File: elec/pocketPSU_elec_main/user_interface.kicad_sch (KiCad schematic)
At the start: 34 parts, among them J3 Conn_01x12_Pin, SW1 EC11E09244BS, U1 2N7002_C5224215

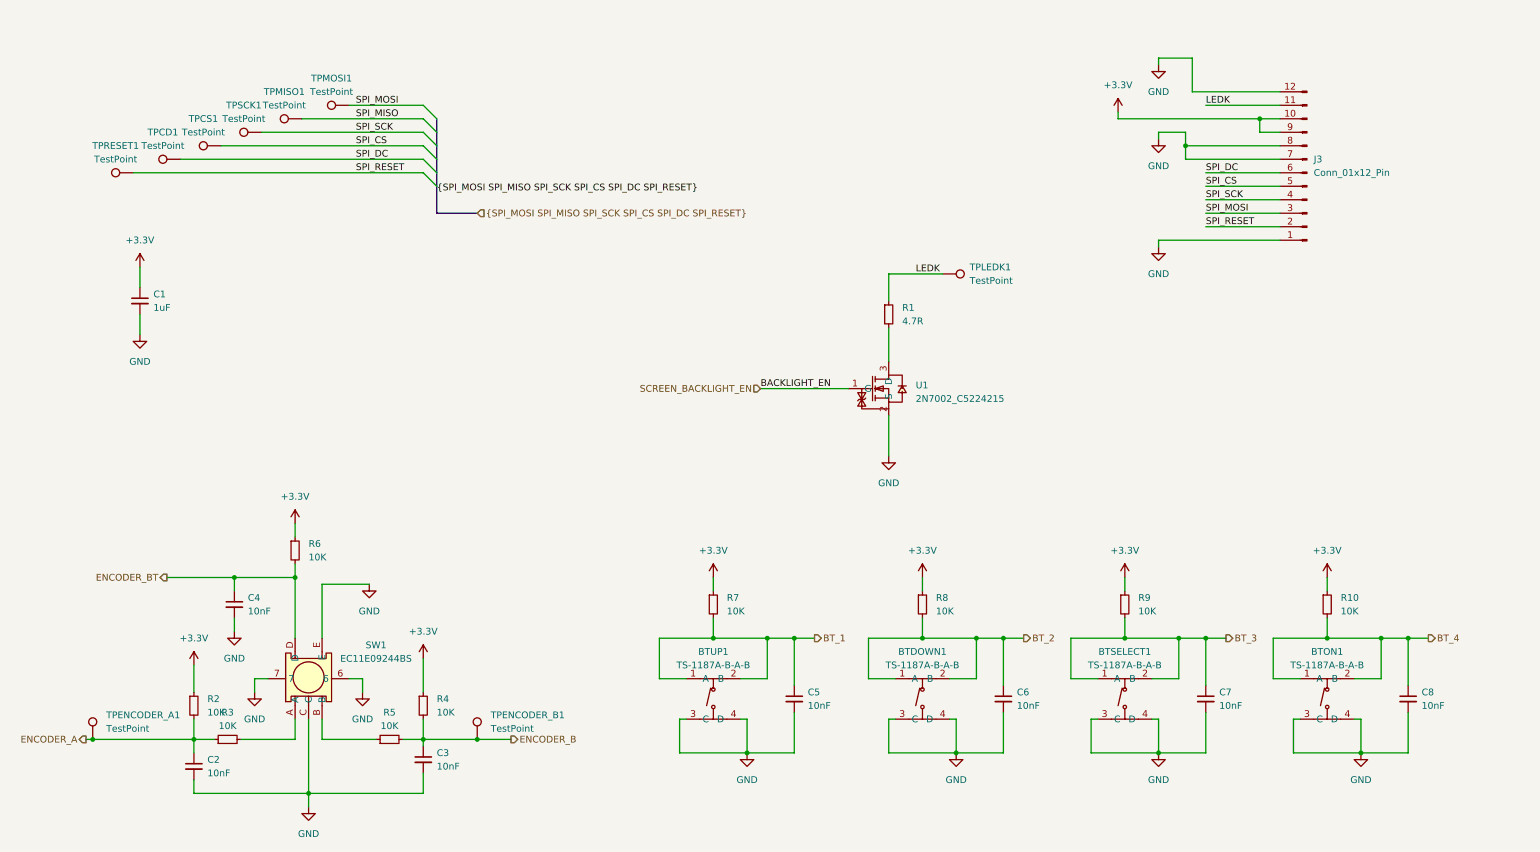
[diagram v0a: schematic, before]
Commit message: add buttons and leds for on/off indication
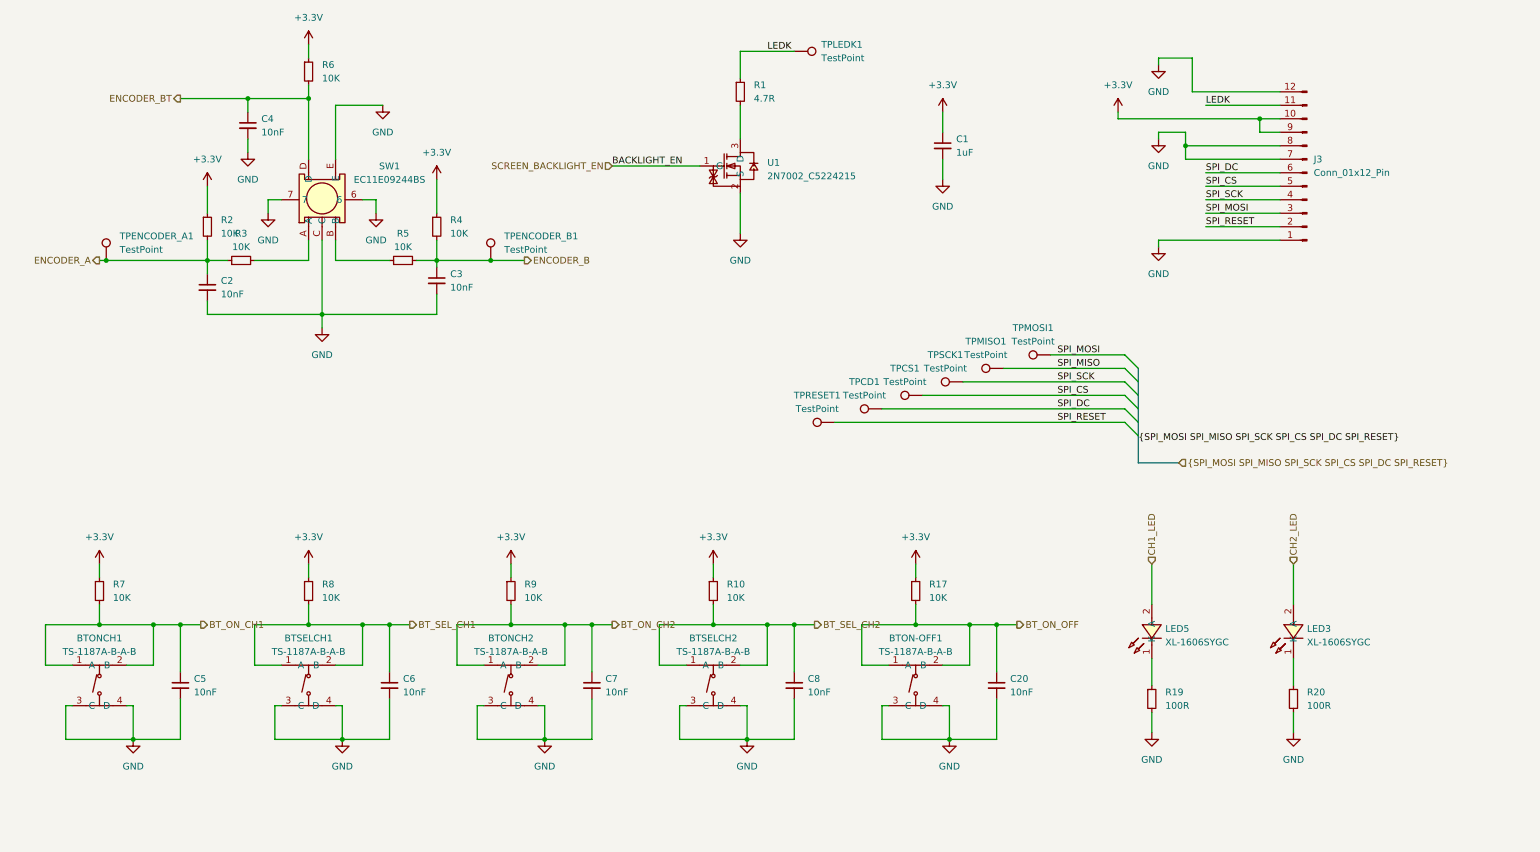
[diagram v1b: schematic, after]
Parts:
- added BTON-OFF1: TS-1187A-B-A-B, footprints:SW-SMD_4P-L5.1-W5.1-P3.70-LS6.5-TL-2, symbol footprints:TS-1187A-B-A-B
- added C20: 10nF, Capacitor_SMD:C_0402_1005Metric, symbol Device:C_Small
- added LED3, LED5: XL-1606SYGC, footprints:LED-SMD_L1.7-W1.1-RD_27-21, symbol footprints:XL-1606SYGC
- added R17: 10K, Resistor_SMD:R_0402_1005Metric, symbol Device:R_Small
- added R19, R20: 100R, Resistor_SMD:R_0402_1005Metric, symbol Device:R_Small
- renumbered BTUP1 to BTONCH1, BTSELECT1 to BTONCH2, BTDOWN1 to BTSELCH1, BTON1 to BTSELCH2
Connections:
- net +3.3V: now also R17.1
- net GND: now also BTON-OFF1.3 (C), BTON-OFF1.4 (D), C20.2, R19.2, R20.2
- net BT_1 renamed BT_ON_CH1
- net BT_2 renamed BT_SEL_CH1
- net BT_3 renamed BT_ON_CH2
- net BT_4 renamed BT_SEL_CH2
- new net: LED3.1 (K), R20.1
- new net: LED5.1 (K), R19.1
- new net BT_ON_OFF: BTON-OFF1.1 (A), BTON-OFF1.2 (B), C20.1, R17.2
- new net CH1_LED: LED5.2 (A)
- new net CH2_LED: LED3.2 (A)
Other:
- moved on the sheet: BTONCH1, BTONCH2, BTSELCH1, BTSELCH2, C1, C2, C3, C4, C5, C6, C7, C8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

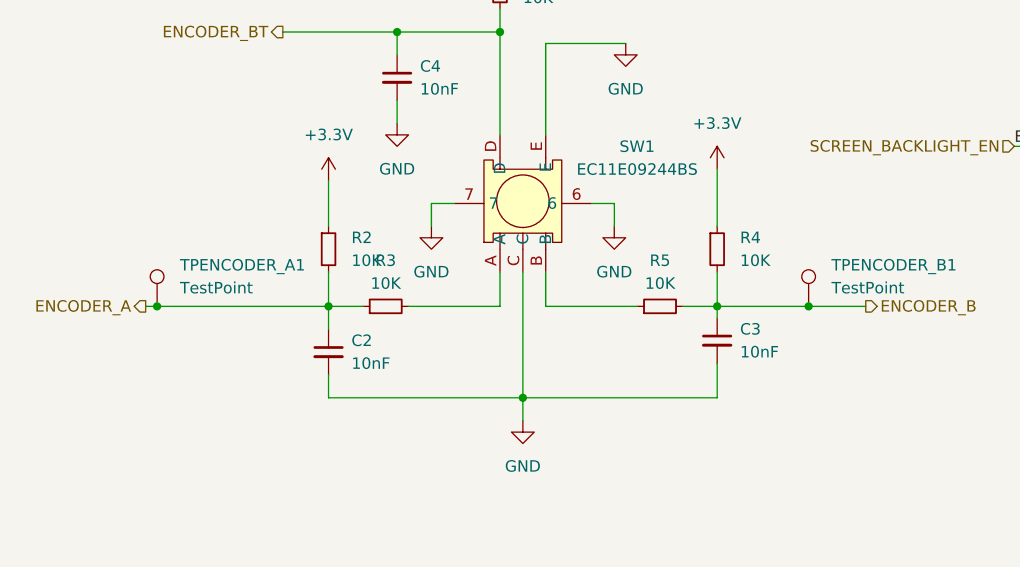
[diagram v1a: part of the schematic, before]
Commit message: move pullup nodes, change to 2.54mm header
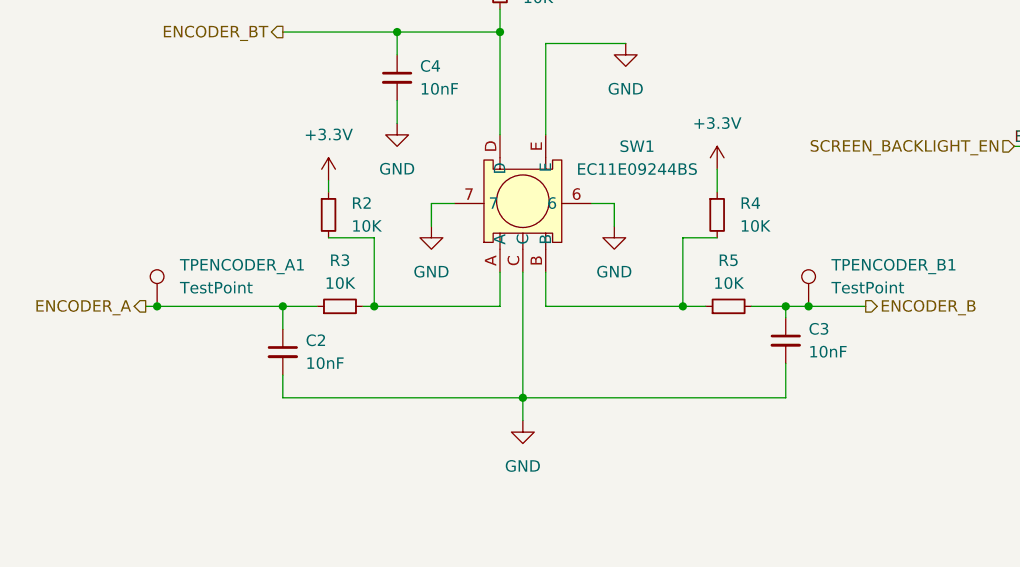
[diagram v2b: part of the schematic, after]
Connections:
- net ENCODER_A: no longer R2.2
- net ENCODER_B: no longer R4.2
- net at R3.2, SW1.A: now also R2.2
- net at R5.1, SW1.B: now also R4.2
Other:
- moved on the sheet: C2, C3, R2, R3, R4, R5

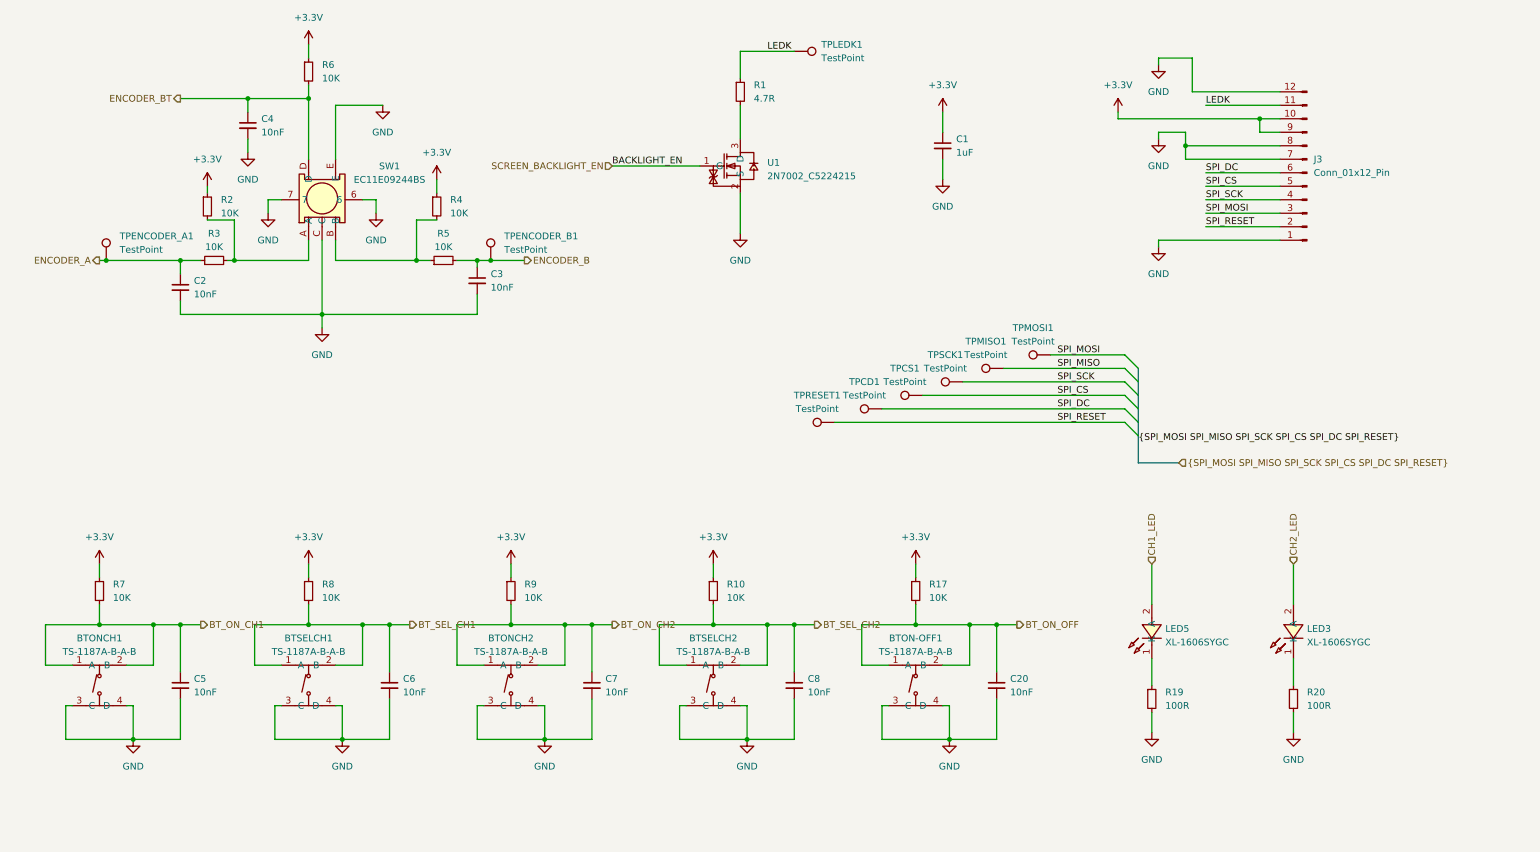
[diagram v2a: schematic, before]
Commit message: Cleanup, Buck, CAN (#6)
* mid-layout

* finished routing

* Kibot (#7)

Add kibot with JLC output generation

* fix 3d, add drc

* fix erc

* fix pcb drc

* drc ignore_unconnected

* attempt to add githash and tag

* add silk githash string

* add silk tag string

* change outputs

---------

Co-authored-by: Jarrod Tuma <jtuma@Jarrods-Laptop.local>
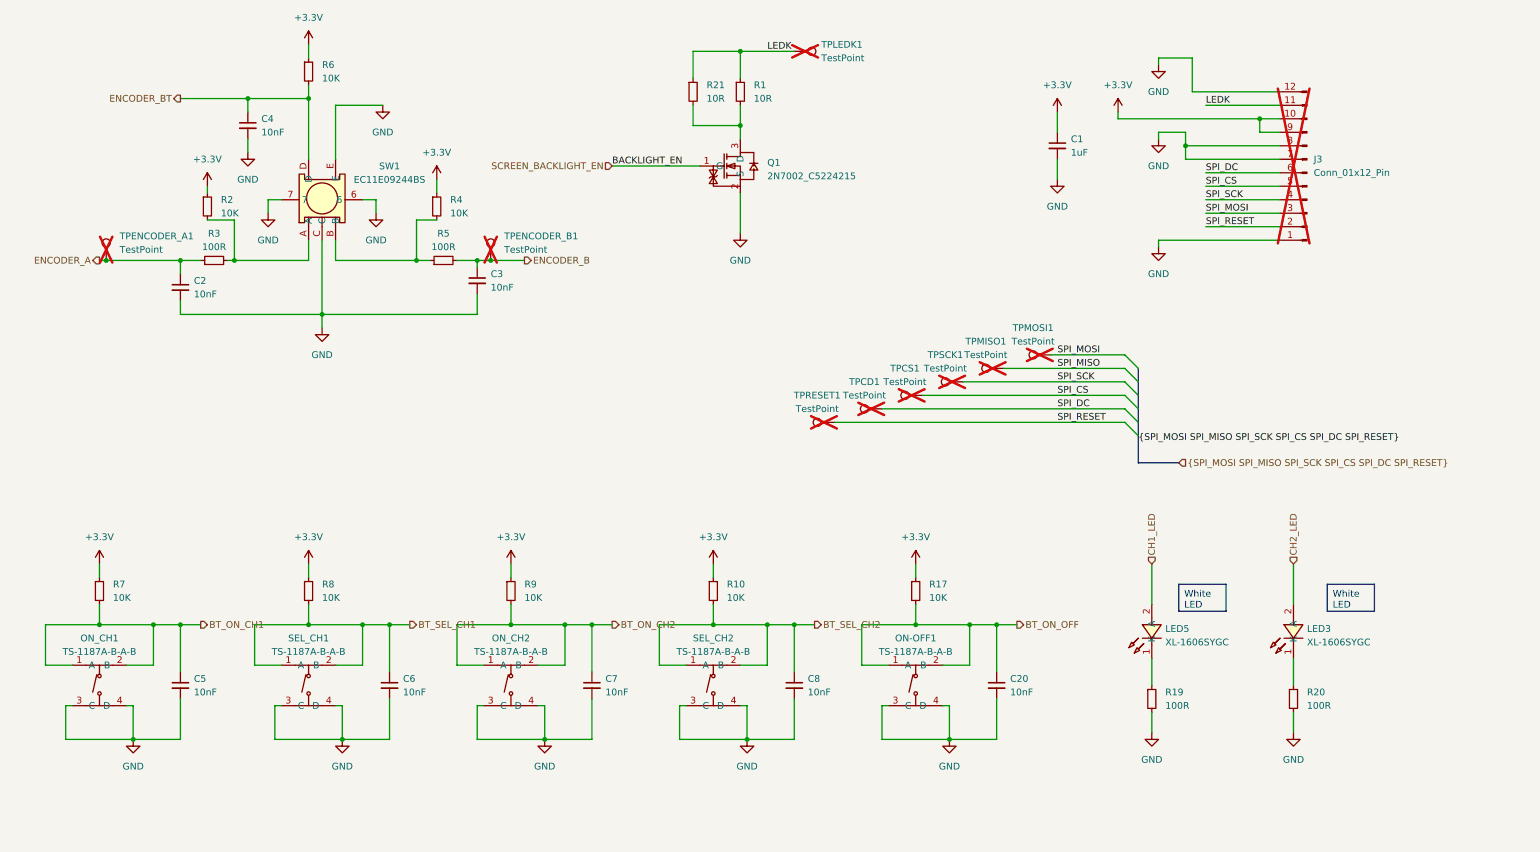
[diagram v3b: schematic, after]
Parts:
- added R21: 10R, Resistor_SMD:R_0402_1005Metric, symbol Device:R_Small
- C1: LCSC Part (none) -> C28323
- C2, C20, C3, C4, C5, C6, C7, C8: LCSC Part (none) -> C15195
- J3, TPCD1, TPCS1, TPENCODER_A1, TPENCODER_B1, TPLEDK1, TPMISO1, TPMOSI1, TPRESET1, TPSCK1: now not fitted
- LED3, LED5: LCSC Part C965864 -> C2290
- R1: value 4.7R -> 10R; LCSC Part (none) -> C25077
- R10, R17, R2, R4, R6, R7, R8, R9: LCSC Part (none) -> C25744
- R19, R20: LCSC Part (none) -> C25076
- R3, R5: value 10K -> 100R; LCSC Part (none) -> C25076
- renumbered BTON-OFF1 to ON-OFF1, BTONCH1 to ON_CH1, BTONCH2 to ON_CH2, U1 to Q1, BTSELCH1 to SEL_CH1, BTSELCH2 to SEL_CH2
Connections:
- net LEDK: now also R21.1
- net at Q1.3 (D), R1.2: now also R21.2
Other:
- moved on the sheet: C1

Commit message: Add mini esp32 module, smd rotary encoder and leds
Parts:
- removed LED3, LED5: XL-1606SYGC, footprints:LED-SMD_L1.7-W1.1-RD_27-21, symbol footprints:XL-1606SYGC
- removed SW1: EC11E09244BS, footprints:SW-TH_EC11XXXXXXXX, symbol footprints:EC11E09244BS
- added LED3, LED4: F.0603.00026/P2-0603B1TS2-06T-001, footprints:LED0603-RD, symbol footprints:F.0603.00026_P2-0603B1TS2-06T-001
- added SW2: EC11J1525402, footprints:SW-SMD_EC11J1525402, symbol footprints:EC11J1525402
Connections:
- net CH1_LED: now also LED4.2 (A)
- net CH2_LED: now also LED3.2 (A)
- net ENCODER_BT: now also SW2.D
- net GND: now also SW2.10, SW2.11, SW2.6, SW2.7, SW2.8, SW2.9, SW2.C, SW2.E
- net at R2.2, R3.2: now also SW2.A
- net at R20.1: now also LED3.1 (K)
- net at R19.1: now also LED4.1 (K)
- net at R4.2, R5.1: now also SW2.B
